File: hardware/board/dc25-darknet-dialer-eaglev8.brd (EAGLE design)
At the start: 101.6 x 101.6 mm, 86 parts, among them SW1 RESET, X1 10118193-0001LF, Y1 RESONATORSMD

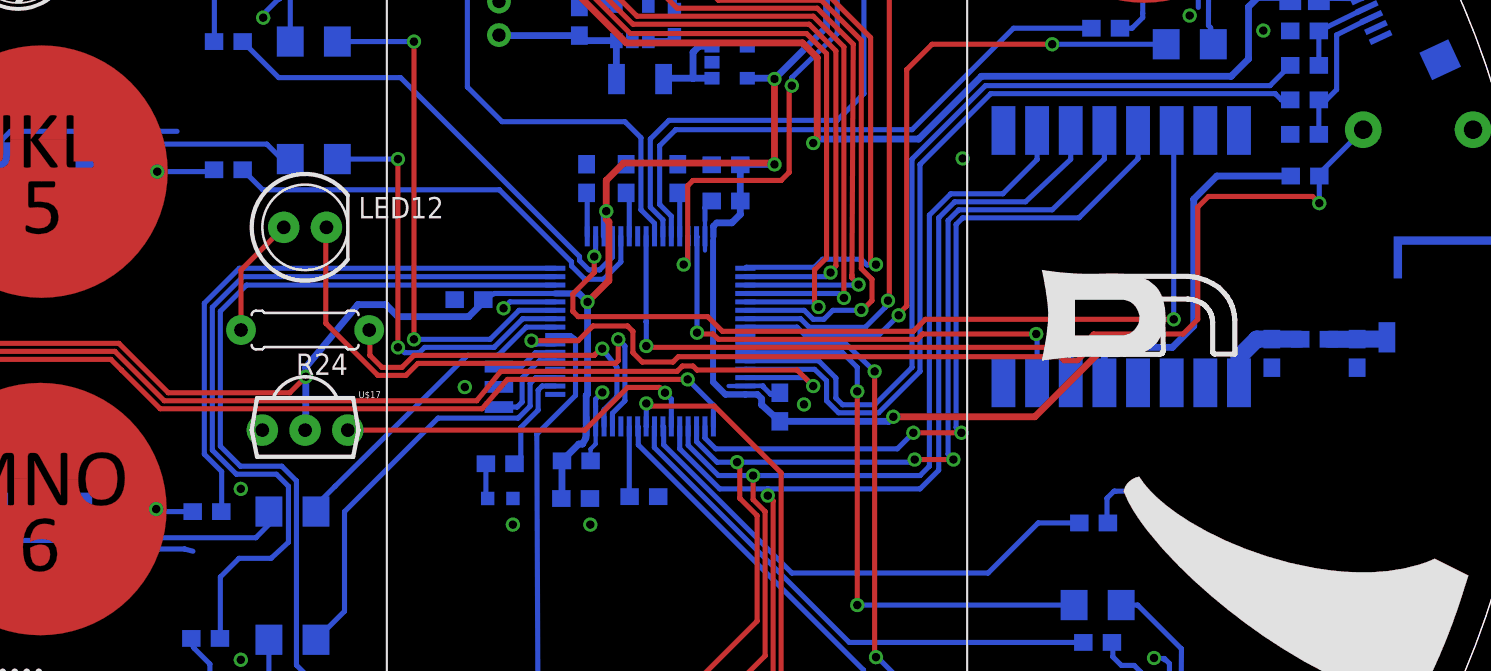
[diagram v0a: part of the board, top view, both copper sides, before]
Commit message: Changed orientation of IR reciver
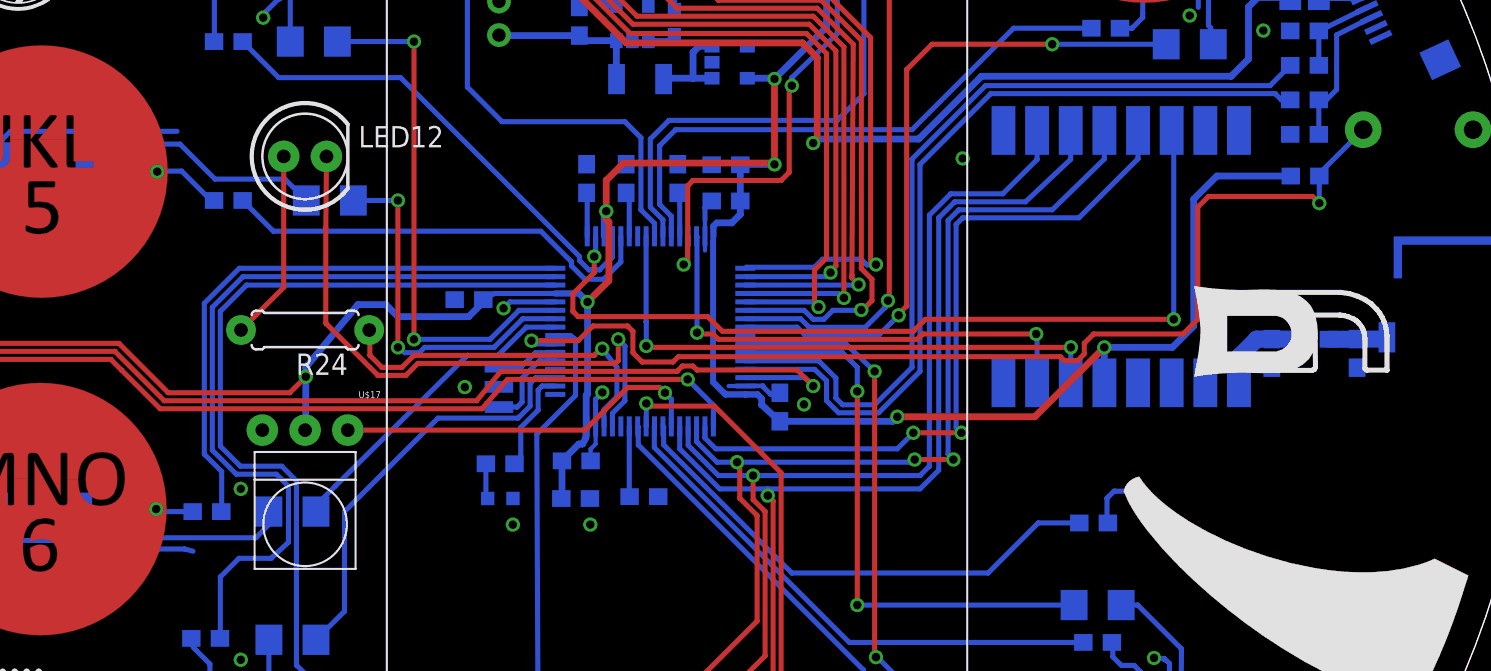
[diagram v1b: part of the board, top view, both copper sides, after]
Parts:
- C17: value (none) -> 1uF
- R1, R10, R2, R3, R4, R5, R6, R7, R8, R9: value (none) -> 47
- R24, R28: value (none) -> 56
- U$17: value SOP22 -> SOP22FLAT; device darknet_parts_library:IR-MODULE -> darknet_parts_library:IR-MODULE_FLAT
- moved U$1 9.10 mm to (81.2, 48.8)
- moved LED12 4.22 mm to (28.7, 61.8)
- moved R5 2.64 mm to (30.2, 59.1)
- moved R15 1.83 mm to (24.1, 59.1)
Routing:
- net N$23: track 7.16 -> 11.4 mm
- net TIM_IR_CARRIER_FREQ: track 31.7 -> 35.9 mm
- net LED5: track 25.2 -> 21.8 mm
- net N$16: track 13.7 -> 15.4 mm
- net TSC_G2_IO2: track 27.3 -> 26.5 mm
- net N$5: track 3.42 -> 4.12 mm

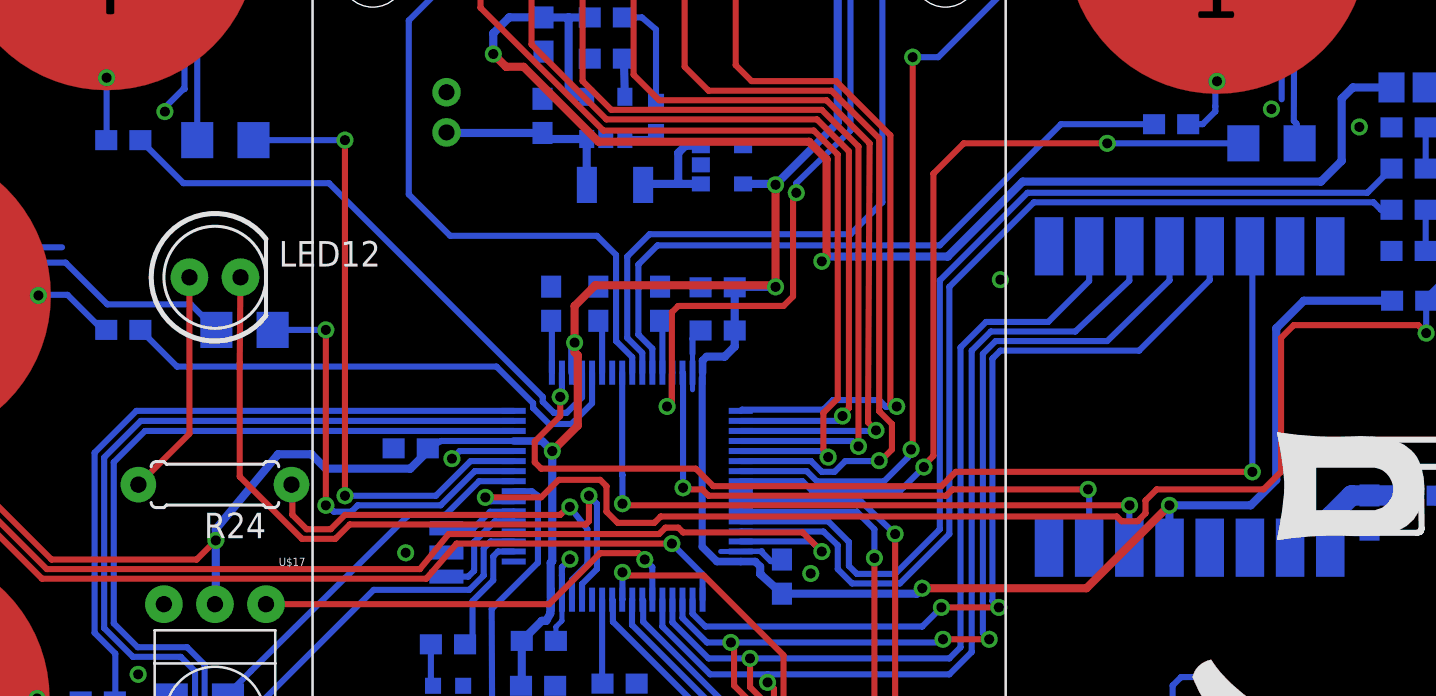
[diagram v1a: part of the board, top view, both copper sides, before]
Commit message: Updated silk screen parts indicators
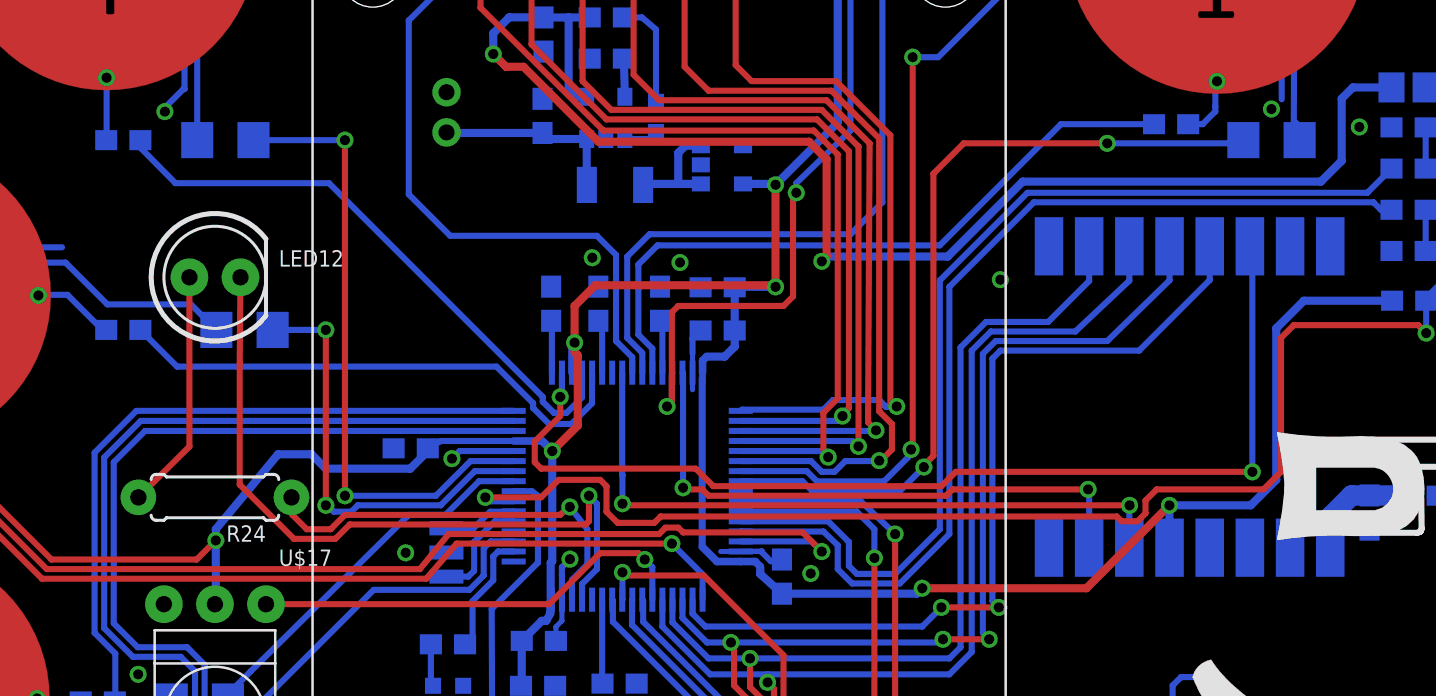
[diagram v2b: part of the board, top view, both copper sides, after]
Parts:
- moved R24 0.63 mm to (28.7, 50.8)
- moved R1 0.16 mm to (81.3, 68.6)
- renumbered SAMPLE_CAP_G1 to C23, SAMPLE_CAP_G2 to C24, SAMPLE_CAP_G3 to C22, SAMPLE_CAP_G5 to C25, U$11 to U2, U$19 to U1
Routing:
- net N$23: track 11.4 -> 12.0 mm
- net IR_OUT: track 21.3 -> 20.7 mm
- net GND: vias 17 -> 19
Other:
- board text added: "RESET"

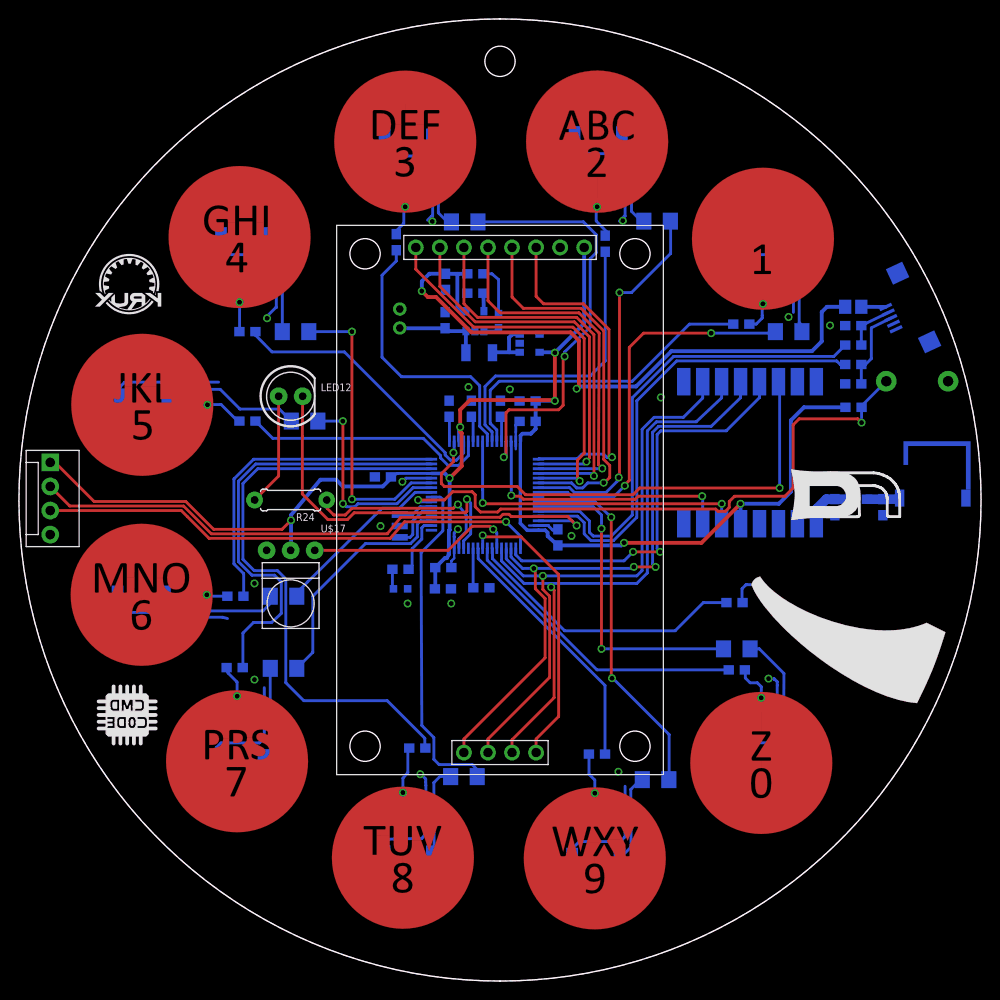
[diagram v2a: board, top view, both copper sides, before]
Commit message: Updated parts for upload to MacroFab
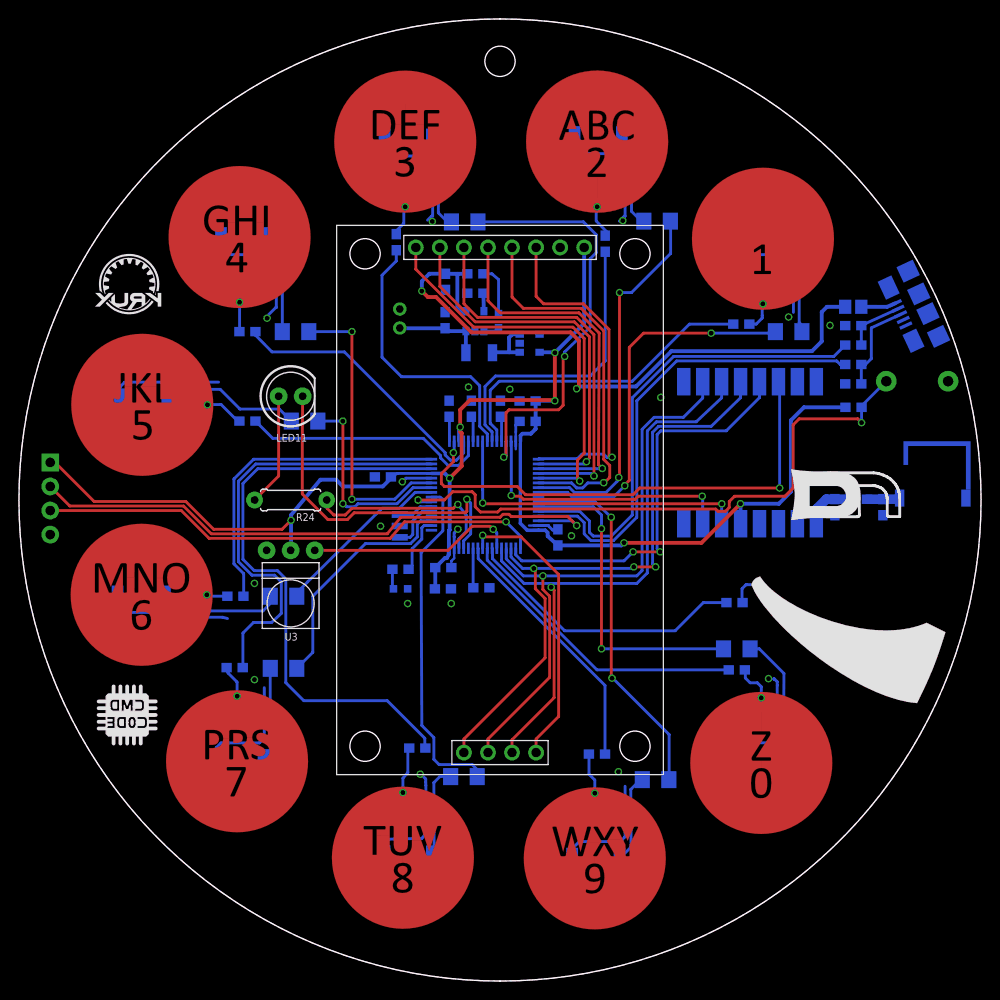
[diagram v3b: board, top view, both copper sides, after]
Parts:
- C1: value 0.5pF -> 251R14S0R5BV4T
- C16: value 4.7uF -> GRM188R61A475ME15D
- C17: value 1uF -> GRM188R61A475ME15D
- C18: value (none) -> GRM188R61A475ME15D
- C19, C20: value 47pF -> C0603C470J3GACTU
- C22, C23, C24, C25: value 0.047uF -> C0603C473J3RACAUTO
- F1: value 500uA -> 0ZCA0050FF2G
- L1: value (none) -> BLM21PG221SN1D
- L2: value 10nH -> CI160808-10NJ
- L3: value 4.7nH -> CI160808-4N7D
- LED11: device SYNShop:LED-0603 -> SYNShop:LED5MM
- LED12: value (none) -> MF-LED-0603-GREEN; device SYNShop:LED5MM -> SYNShop:LED-0603
- LED13: value (none) -> MF-LED-0603-GREEN
- R1, R10, R2, R3, R4, R5, R6, R7, R8, R9: value 47 -> CRCW120647R0JNEA
- R22: value (none) -> 2K
- R23: value (none) -> 470
- R24: value 56 -> 47
- R25: value (none) -> 10K
- R28: value 56 -> 68
- U$2: value STM32F302XC -> STM32F302RBT6
- U$21: value CHIP_ANTENNA -> 0915AT43A0026E
- U1: value TLV702 -> BU33SD5WG-TR
- U2: value DS21984E -> MCP73831T-5ACI/OT
- Y1: value RESONATORSMD -> CSTCE8M00G52-R0
- moved LED11 23.4 mm to (28.7, 61.8), flipped to the top, turned to 0 degrees
- moved LED12 23.4 mm to (50.6, 69.7), flipped to the bottom, turned to 180 degrees
- moved X1 1.11 mm to (95.5, 71.5)
- flipped STLINK to the bottom
- renumbered U$17 to U3
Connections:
- net N$23: now also LED11.A; no longer LED12.A
- net N$24: now also LED12.A; no longer LED11.A
- net N$25: now also LED12.C; no longer LED11.C
- net TIM_IR_CARRIER_FREQ: now also LED11.K; no longer LED12.K
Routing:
- net N$28: track 2.57 -> 3.68 mm
- net N$27: track 5.21 -> 6.32 mm
- net N$26: track 8.92 -> 10.0 mm

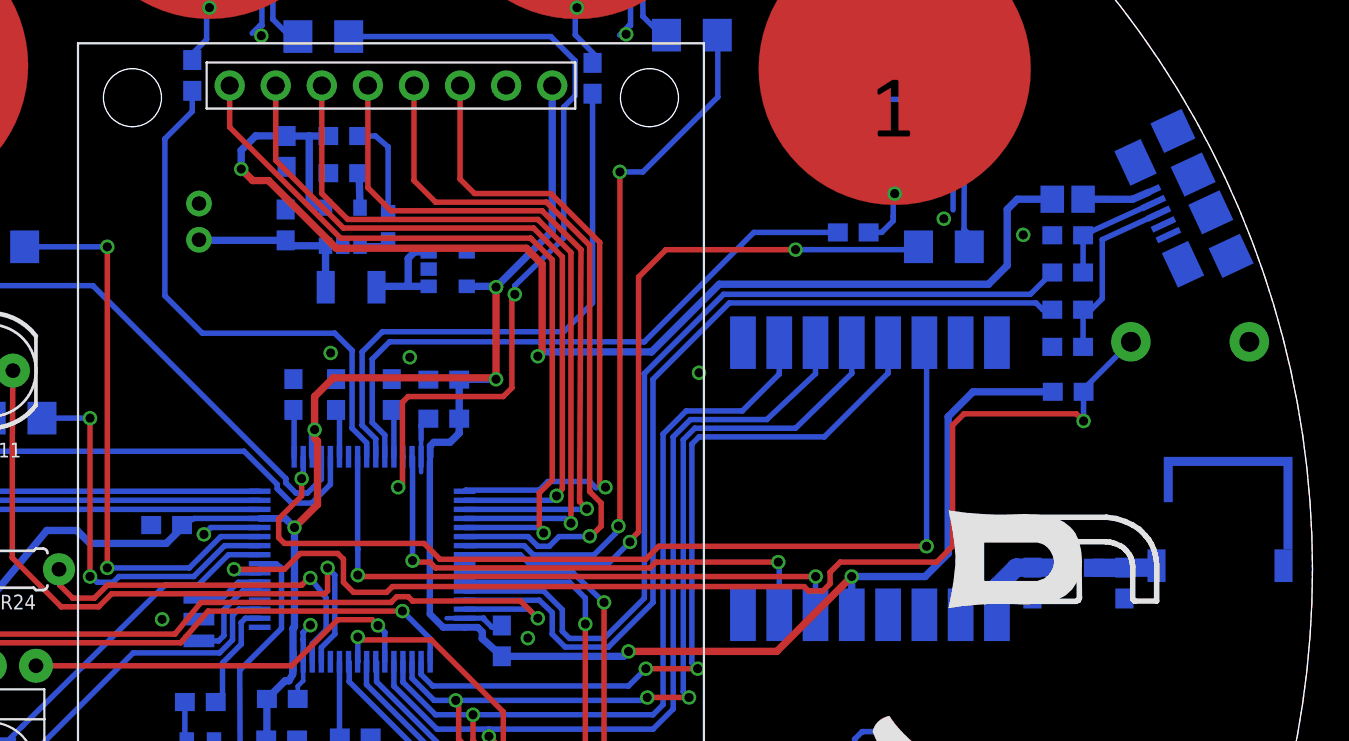
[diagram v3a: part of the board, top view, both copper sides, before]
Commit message: Changed USB connector to Macrofab eagle library
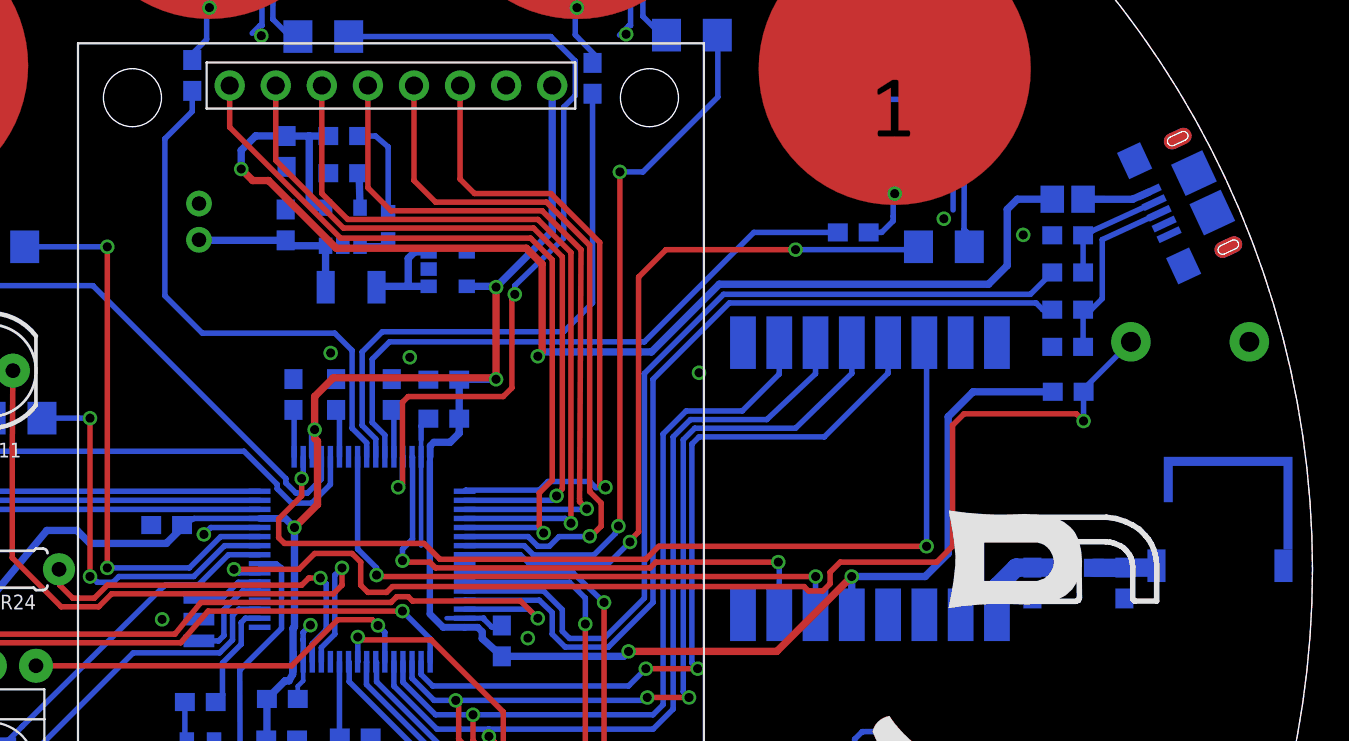
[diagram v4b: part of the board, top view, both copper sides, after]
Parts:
- removed X1: 10118193-0001LF, SYNShop:USB-MICROB
- added J1: MF-CON-MICROUSB-RIGHT, MF_Connectors:MICROUSB-RIGHT
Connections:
- net GND: now also J1.5, J1.S1, J1.S2, J1.S3, J1.S4, J1.S5, J1.S6; no longer X1.GND
- net N$26: now also J1.3; no longer X1.D+
- net N$27: now also J1.2; no longer X1.D-
- net N$28: now also J1.1; no longer X1.VBUS
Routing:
- net GND: track 143.8 -> 147.9 mm
- net RMF69_INTERRUPT_DIO1: track 29.1 -> 29.9 mm
- net TIM_IR_CARRIER_FREQ: track 36.1 -> 36.7 mm
- net RMF69_INTERRUPT_DIO0: track 33.9 -> 33.3 mm
